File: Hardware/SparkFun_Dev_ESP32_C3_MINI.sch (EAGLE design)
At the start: 41 parts, among them J1 USB Female Type C Connector, J5 Vertical Qwiic Connector, U1 ESP32-C3_MINI-1, U2 RT9080-33GJ5

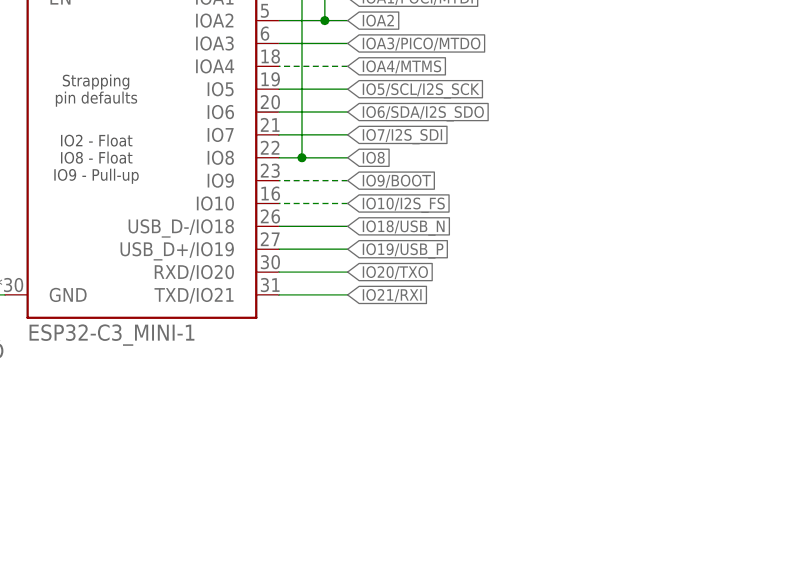
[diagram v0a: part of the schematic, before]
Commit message: Fixes UART lines at module
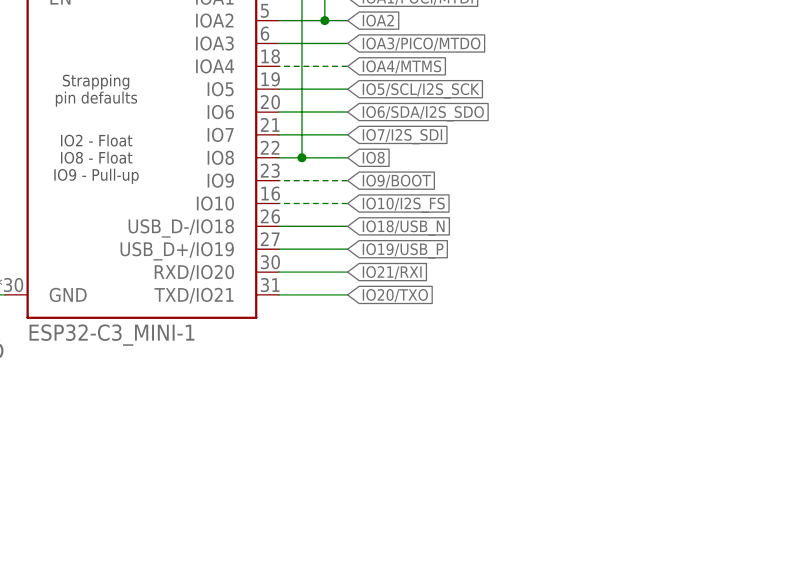
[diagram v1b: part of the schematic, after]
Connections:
- net IO20/TXO: now also U1.TXD/IO21; no longer U1.RXD/IO20
- net IO21/RXI: now also U1.RXD/IO20; no longer U1.TXD/IO21
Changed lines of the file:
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@@
 <setting verticaltext="up"/>
 </settings>
-<grid distance="0.5" unitdist="mm" unit="mm" style="lines" multiple="1" display="yes" altdistance="0.01" altunitdist="mm" altunit="mm"/>
+<grid distance="0.1" unitdist="inch" unit="inch" style="lines" multiple="1" display="no" altdistance="0.01" altunitdist="inch" altunit="inch"/>
 <layers>
 <layer number="1" name="Top" color="4" fill="1" visible="no" active="no"/>
@@
 <net name="IO21/RXI" class="0">
 <segment>
+<wire x1="391.16" y1="139.7" x2="396.24" y2="139.7" width="0.1524" layer="91"/>
+<label x="396.24" y="139.7" size="1.27" layer="95" font="vector" xref="yes"/>
+<pinref part="U$2" gate="G$1" pin="8"/>
+</segment>
+<segment>
+<wire x1="678.18" y1="200.66" x2="685.8" y2="200.66" width="0.1524" layer="91"/>
+<label x="685.8" y="200.66" size="1.27" layer="95" font="vector" xref="yes"/>
+<pinref part="U1" gate="G$1" pin="RXD/IO20"/>
+</segment>
+</net>
+<net name="IO20/TXO" class="0">
+<segment>
+<wire x1="391.16" y1="142.24" x2="396.24" y2="142.24" width="0.1524" layer="91"/>
+<label x="396.24" y="142.24" size="1.27" layer="95" font="vector" xref="yes"/>
+<pinref part="U$2" gate="G$1" pin="9"/>
+</segment>
+<segment>
 <wire x1="678.18" y1="198.12" x2="685.8" y2="198.12" width="0.1524" layer="91"/>
 <label x="685.8" y="198.12" size="1.27" layer="95" font="vector" xref="yes"/>
 <pinref part="U1" gate="G$1" pin="TXD/IO21"/>
 </segment>
-<segment>
-<wire x1="391.16" y1="139.7" x2="396.24" y2="139.7" width="0.1524" layer="91"/>
-<label x="396.24" y="139.7" size="1.27" layer="95" font="vector" xref="yes"/>
-<pinref part="U$2" gate="G$1" pin="8"/>
-</segment>
-</net>
-<net name="IO20/TXO" class="0">
-<segment>
-<wire x1="678.18" y1="200.66" x2="685.8" y2="200.66" width="0.1524" layer="91"/>
-<label x="685.8" y="200.66" size="1.27" layer="95" font="vector" xref="yes"/>
-<pinref part="U1" gate="G$1" pin="RXD/IO20"/>
-</segment>
-<segment>
-<wire x1="391.16" y1="142.24" x2="396.24" y2="142.24" width="0.1524" layer="91"/>
-<label x="396.24" y="142.24" size="1.27" layer="95" font="vector" xref="yes"/>
-<pinref part="U$2" gate="G$1" pin="9"/>
-</segment>
-</net>
+</net>

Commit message: Updates symbol to include correct JTAG interface
* Updates nets to reflect JTAG correction, moves JTAG header and routes new JTAG connection
* Updates silk for fix above
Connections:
- removed net IO5/SCL/I2S_SCK: J5.4, R4.2, U$2.4, U1.IO5
- removed net IO6/SDA/I2S_SDO: J5.3, R3.1, U$2.5, U1.IO6
- removed net IO7/I2S_SDI: U$2.3, U1.IO7
- removed net IOA0/SCLK/MTCK: TP3.1, U$3.7, U1.IOA0
- removed net IOA1/POCI/MTDI: TP6.1, U$3.6, U1.IOA1
- removed net IOA3/PICO/MTDO: TP1.1, U$3.5, U1.IOA3
- new net IO5/SDA/I2S_SDI/MTDI: J5.3, R4.2, TP6.1, U$2.5, U1.IO5/MTDI
- new net IO6/SCL/I2S_SCK/MTCK: J5.4, R3.1, TP3.1, U$2.4, U1.IO6/MTCK
- new net IO7/I2S_SDO/MTDO: TP1.1, U$2.3, U1.IO7/MTDO
- new net IOA0/SCLK: U$3.7, U1.IOA0
- new net IOA1/POCI: U$3.6, U1.IOA1
- new net IOA3/PICO: U$3.5, U1.IOA3
- net IOA4/MTMS: now also U1.IOA4/MTMS; no longer U1.IOA4
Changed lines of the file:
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@@
 </segment>
 </net>
-<net name="IOA3/PICO/MTDO" class="0">
+<net name="IOA3/PICO" class="0">
 <segment>
 <wire x1="685.8" y1="226.06" x2="678.18" y2="226.06" width="0.1524" layer="91"/>
@@
 <pinref part="U$3" gate="G$1" pin="5"/>
 </segment>
-<segment>
-<wire x1="406.4" y1="27.94" x2="403.86" y2="27.94" width="0.1524" layer="91" style="longdash"/>
-<label x="403.86" y="27.94" size="1.27" layer="95" font="vector" rot="MR0" xref="yes"/>
-<pinref part="TP1" gate="G$1" pin="1"/>
-</segment>
 </net>
-<net name="IOA1/POCI/MTDI" class="0">
+<net name="IOA1/POCI" class="0">
 <segment>
 <wire x1="685.8" y1="231.14" x2="678.18" y2="231.14" width="0.1524" layer="91" style="longdash"/>
@@
 <label x="436.88" y="129.54" size="1.27" layer="95" font="vector" rot="R180" xref="yes"/>
 <pinref part="U$3" gate="G$1" pin="6"/>
-</segment>
-<segment>
-<wire x1="421.64" y1="27.94" x2="419.1" y2="27.94" width="0.1524" layer="91" style="longdash"/>
-<label x="421.64" y="27.94" size="1.27" layer="95" font="vector" xref="yes"/>
-<pinref part="TP6" gate="G$1" pin="1"/>
-</segment>
-</net>
-<net name="IOA0/SCLK/MTCK" class="0">
-<segment>
-<wire x1="685.8" y1="233.68" x2="678.18" y2="233.68" width="0.1524" layer="91" style="longdash"/>
-<label x="685.8" y="233.68" size="1.27" layer="95" font="vector" xref="yes"/>
-<pinref part="U1" gate="G$1" pin="IOA0"/>
-</segment>
-<segment>
-<wire x1="436.88" y1="127" x2="444.5" y2="127" width="0.1524" layer="91"/>
-<label x="436.88" y="127" size="1.27" layer="95" font="vector" rot="R180" xref="yes"/>
-<pinref part="U$3" gate="G$1" pin="7"/>
-</segment>
-<segment>
-<pinref part="TP3" gate="G$1" pin="1"/>
-<wire x1="406.4" y1="17.78" x2="401.32" y2="17.78" width="0.1524" layer="91" style="longdash"/>
-<label x="401.32" y="17.78" size="1.27" layer="95" font="vector" rot="MR0" xref="yes"/>
 </segment>
 </net>
@@
 <wire x1="685.8" y1="223.52" x2="678.18" y2="223.52" width="0.1524" layer="91" style="longdash"/>
 <label x="685.8" y="223.52" size="1.27" layer="95" font="vector" xref="yes"/>
-<pinref part="U1" gate="G$1" pin="IOA4"/>
+<pinref part="U1" gate="G$1" pin="IOA4/MTMS"/>
 </segment>
 <segment>
@@
 </segment>
 </net>
-<net name="IO5/SCL/I2S_SCK" class="0">
-<segment>
-<wire x1="426.72" y1="76.2" x2="421.64" y2="76.2" width="0.1524" layer="91"/>
-<label x="426.72" y="76.2" size="1.27" layer="95" font="vector" xref="yes"/>
-<pinref part="J5" gate="J1" pin="4"/>
-</segment>
+<net name="IO5/SDA/I2S_SDI/MTDI" class="0">
 <segment>
 <wire x1="685.8" y1="220.98" x2="678.18" y2="220.98" width="0.1524" layer="91"/>
 <label x="685.8" y="220.98" size="1.27" layer="95" font="vector" xref="yes"/>
-<pinref part="U1" gate="G$1" pin="IO5"/>
+<pinref part="U1" gate="G$1" pin="IO5/MTDI"/>
 </segment>
 <segment>
@@
 </segment>
 <segment>
-<wire x1="396.24" y1="129.54" x2="391.16" y2="129.54" width="0.1524" layer="91"/>
-<label x="396.24" y="129.54" size="1.27" layer="95" font="vector" xref="yes"/>
-<pinref part="U$2" gate="G$1" pin="4"/>
+<wire x1="396.24" y1="132.08" x2="391.16" y2="132.08" width="0.1524" layer="91"/>
+<label x="396.24" y="132.08" size="1.27" layer="95" font="vector" xref="yes"/>
+<pinref part="U$2" gate="G$1" pin="5"/>
 </segment>
-</net>
-<net name="IO6/SDA/I2S_SDO" class="0">
 <segment>
-<wire x1="421.64" y1="73.66" x2="426.72" y2="73.66" width="0.1524" layer="91"/>
+<wire x1="426.72" y1="73.66" x2="421.64" y2="73.66" width="0.1524" layer="91"/>
 <label x="426.72" y="73.66" size="1.27" layer="95" font="vector" xref="yes"/>
 <pinref part="J5" gate="J1" pin="3"/>
 </segment>
 <segment>
+<wire x1="421.64" y1="27.94" x2="419.1" y2="27.94" width="0.1524" layer="91" style="longdash"/>
+<label x="421.64" y="27.94" size="1.27" layer="95" font="vector" xref="yes"/>
+<pinref part="TP6" gate="G$1" pin="1"/>
+</segment>
+</net>
+<net name="IO6/SCL/I2S_SCK/MTCK" class="0">
+<segment>
 <wire x1="685.8" y1="218.44" x2="678.18" y2="218.44" width="0.1524" layer="91"/>
 <label x="685.8" y="218.44" size="1.27" layer="95" font="vector" xref="yes"/>
-<pinref part="U1" gate="G$1" pin="IO6"/>
+<pinref part="U1" gate="G$1" pin="IO6/MTCK"/>
 </segment>
 <segment>
@@
 </segment>
 <segment>
-<wire x1="396.24" y1="132.08" x2="391.16" y2="132.08" width="0.1524" layer="91"/>
-<label x="396.24" y="132.08" size="1.27" layer="95" font="vector" rot="MR180" xref="yes"/>
-<pinref part="U$2" gate="G$1" pin="5"/>
+<wire x1="396.24" y1="129.54" x2="391.16" y2="129.54" width="0.1524" layer="91"/>
+<label x="396.24" y="129.54" size="1.27" layer="95" font="vector" rot="MR180" xref="yes"/>
+<pinref part="U$2" gate="G$1" pin="4"/>
+</segment>
+<segment>
+<pinref part="TP3" gate="G$1" pin="1"/>
+<wire x1="406.4" y1="17.78" x2="401.32" y2="17.78" width="0.1524" layer="91" style="longdash"/>
+<label x="401.32" y="17.78" size="1.27" layer="95" font="vector" rot="MR0" xref="yes"/>
+</segment>
+<segment>
+<wire x1="421.64" y1="76.2" x2="426.72" y2="76.2" width="0.1524" layer="91"/>
+<label x="426.72" y="76.2" size="1.27" layer="95" font="vector" xref="yes"/>
+<pinref part="J5" gate="J1" pin="4"/>
 </segment>
 </net>
-<net name="IO7/I2S_SDI" class="0">
+<net name="IO7/I2S_SDO/MTDO" class="0">
 <segment>
 <wire x1="396.24" y1="127" x2="391.16" y2="127" width="0.1524" layer="91"/>
@@
 <wire x1="685.8" y1="215.9" x2="678.18" y2="215.9" width="0.1524" layer="91"/>
 <label x="685.8" y="215.9" size="1.27" layer="95" font="vector" xref="yes"/>
-<pinref part="U1" gate="G$1" pin="IO7"/>
+<pinref part="U1" gate="G$1" pin="IO7/MTDO"/>
+</segment>
+<segment>
+<wire x1="406.4" y1="27.94" x2="403.86" y2="27.94" width="0.1524" layer="91" style="longdash"/>
+<label x="403.86" y="27.94" size="1.27" layer="95" font="vector" rot="MR0" xref="yes"/>
+<pinref part="TP1" gate="G$1" pin="1"/>
 </segment>
 </net>
+<net name="IOA0/SCLK" class="0">
+<segment>
+<wire x1="436.88" y1="127" x2="444.5" y2="127" width="0.1524" layer="91"/>
+<label x="436.88" y="127" size="1.27" layer="95" font="vector" rot="R180" xref="yes"/>
+<pinref part="U$3" gate="G$1" pin="7"/>
+</segment>
+<segment>
+<wire x1="685.8" y1="233.68" x2="678.18" y2="233.68" width="0.1524" layer="91" style="longdash"/>
+<label x="685.8" y="233.68" size="1.27" layer="95" font="vector" xref="yes"/>
+<pinref part="U1" gate="G$1" pin="IOA0"/>
+</segment>
+</net>

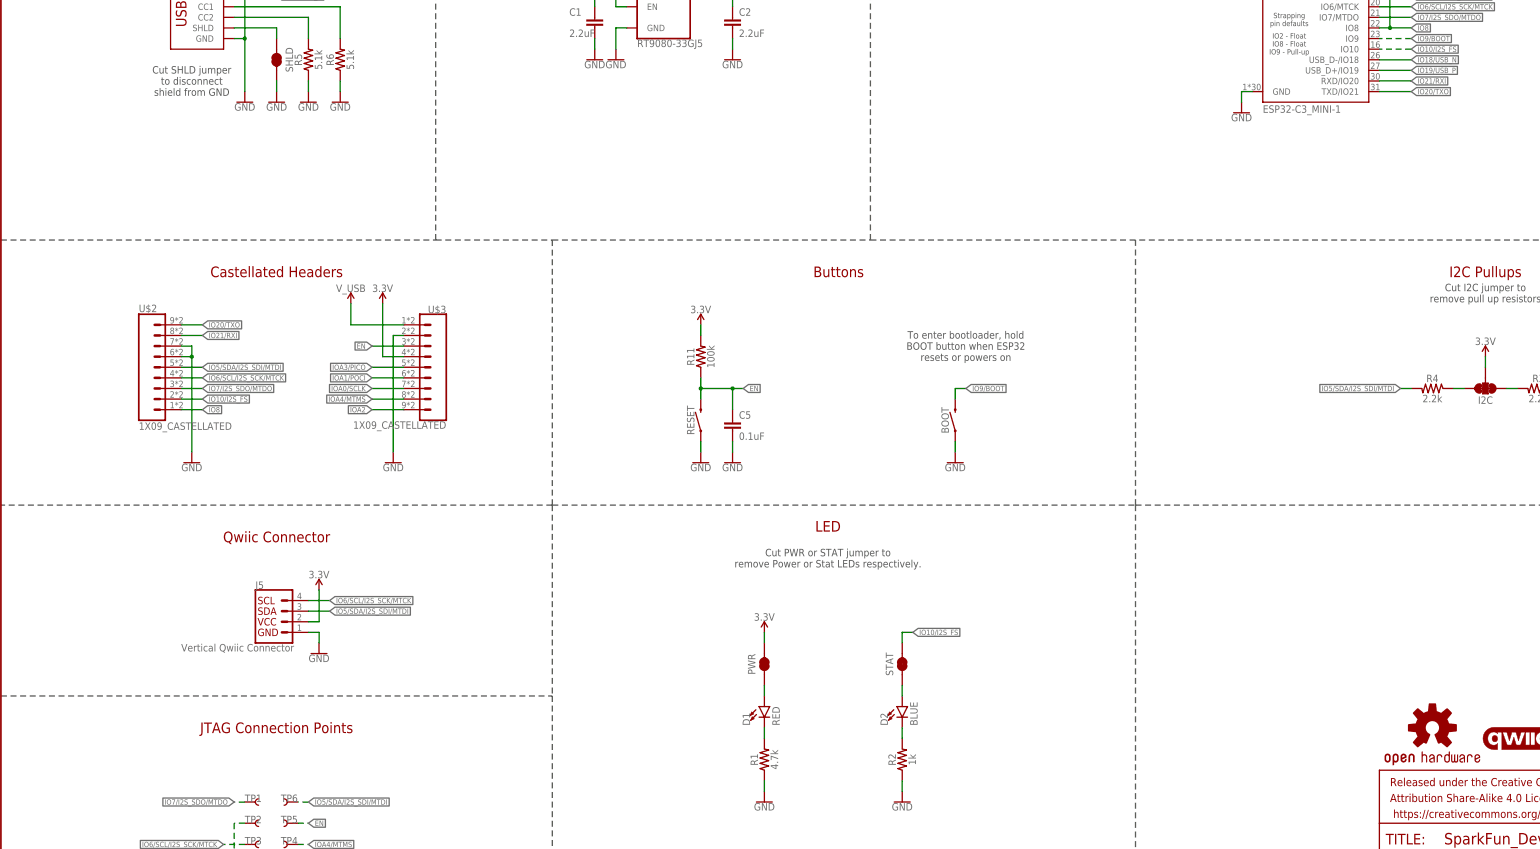
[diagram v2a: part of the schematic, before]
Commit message: Fixes castellation, adds removeable tab
* Reduces minimum annular ring to 3mil
* Adds silk to removeable tag
* Changes "EN" silk to "RST"
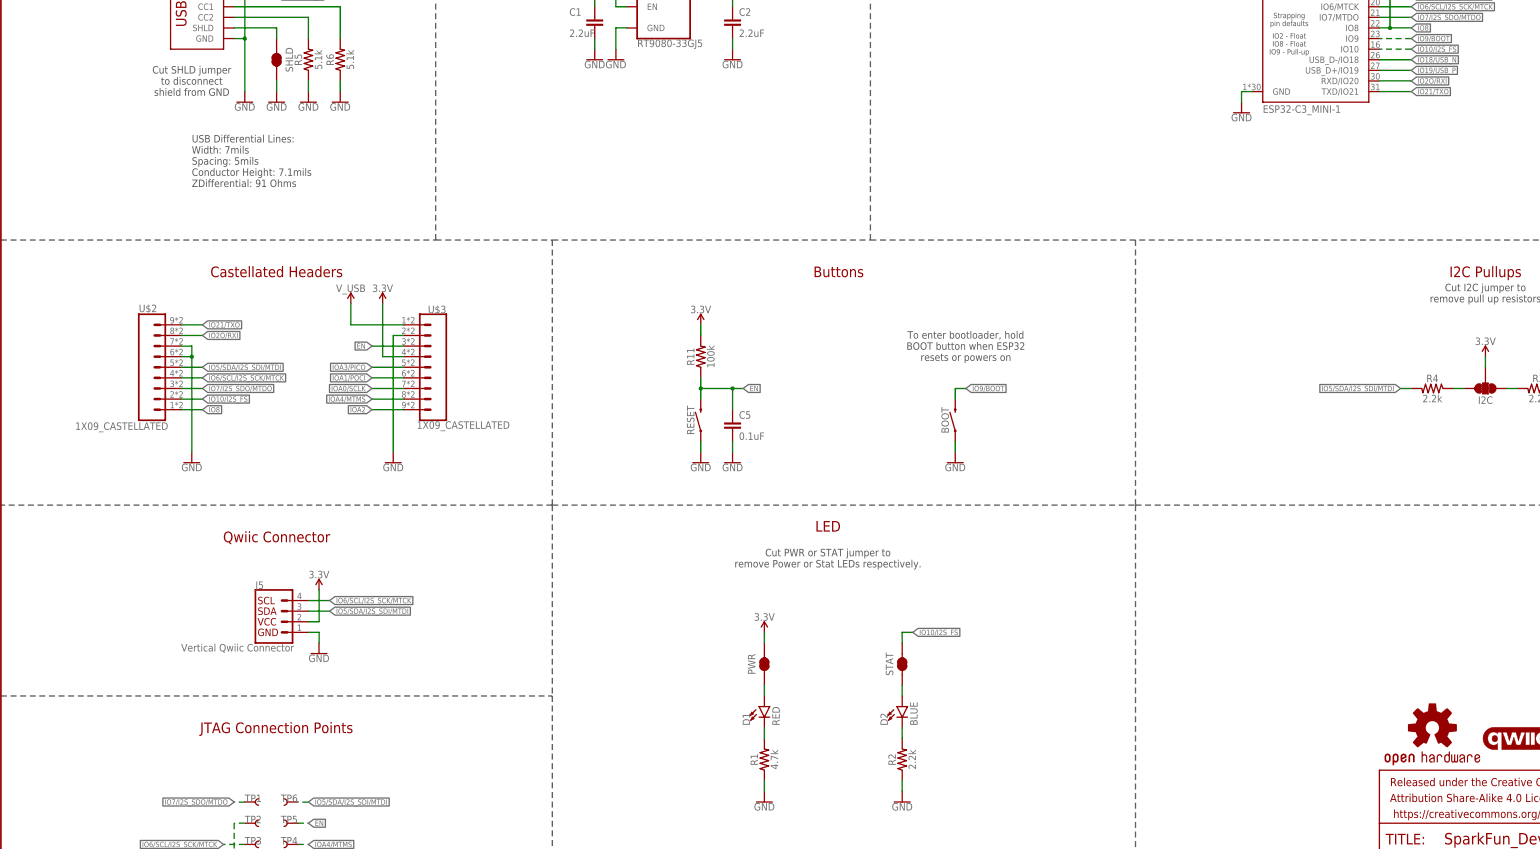
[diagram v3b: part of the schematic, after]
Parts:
- R2: value 1k -> 2.2k; device SparkFun-Resistors:1KOHM-0402T-1/16W-1% -> SparkFun-Resistors:2.2KOHM-0402T-1/16W-1%
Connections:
- net IO20/TXO renamed IO21/TXO
- net IO21/RXI renamed IO2O/RXI
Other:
- note added: "USB Differential Lines: Width: 7mils Spacing: 5mils Conductor Height: 7.1mils ZDifferential: 91 Ohms"
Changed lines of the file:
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@@
 <clearance class="1" value="0.1778"/>
 </class>
-<class number="2" name="USB" width="0.254" drill="0">
-<clearance class="2" value="0.1016"/>
+<class number="2" name="USB" width="0.1778" drill="0">
+<clearance class="2" value="0.127"/>
 </class>
 </classes>
@@
 </part>
 <part name="D2" library="SparkFun-LED" deviceset="LED-BLUE" device="0603" value="BLUE"/>
-<part name="R2" library="SparkFun-Resistors" deviceset="1KOHM" device="-0402T-1/16W-1%" value="1k"/>
+<part name="R2" library="SparkFun-Resistors" deviceset="2.2KOHM" device="-0402T-1/16W-1%" value="2.2k"/>
 <part name="STAT" library="SparkFun-Jumpers" deviceset="JUMPER-SMT_2_NC_TRACE" device="_SILK" package3d_urn="urn:adsk.eagle:package:39281/1"/>
 <part name="GND8" library="SparkFun-PowerSymbols" deviceset="GND" device=""/>
@@
 <wire x1="347.98" y1="53.34" x2="480.06" y2="53.34" width="0.2032" layer="97" style="longdash"/>
 <wire x1="480.06" y1="99.06" x2="347.98" y2="99.06" width="0.2032" layer="97" style="longdash"/>
+<text x="393.7" y="175.26" size="1.778" layer="97" font="vector">USB Differential Lines:
+Width: 7mils
+Spacing: 5mils
+Conductor Height: 7.1mils
+ZDifferential: 91 Ohms </text>
 </plain>
 <instances>
@@
 </instance>
 <instance part="U$2" gate="G$1" x="381" y="132.08" smashed="yes">
-<attribute name="VALUE" x="381" y="117.094" size="1.778" layer="96" font="vector"/>
+<attribute name="VALUE" x="365.76" y="117.094" size="1.778" layer="96" font="vector"/>
 <attribute name="NAME" x="381" y="145.288" size="1.778" layer="95" font="vector"/>
 </instance>
 <instance part="U$3" gate="G$1" x="454.66" y="132.08" smashed="yes" rot="R180">
-<attribute name="VALUE" x="454.66" y="119.126" size="1.778" layer="96" font="vector" rot="R180"/>
+<attribute name="VALUE" x="469.9" y="119.126" size="1.778" layer="96" font="vector" rot="R180"/>
 <attribute name="NAME" x="454.66" y="146.812" size="1.778" layer="95" font="vector" rot="R180"/>
 </instance>
@@
 </segment>
 </net>
-<net name="IO21/RXI" class="0">
+<net name="IO2O/RXI" class="0">
 <segment>
 <wire x1="391.16" y1="139.7" x2="396.24" y2="139.7" width="0.1524" layer="91"/>
@@
 </segment>
 </net>
-<net name="IO20/TXO" class="0">
+<net name="IO21/TXO" class="0">
 <segment>
 <wire x1="391.16" y1="142.24" x2="396.24" y2="142.24" width="0.1524" layer="91"/>
